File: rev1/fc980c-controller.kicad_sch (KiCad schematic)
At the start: 35 parts, among them J1 SWD, J2 USB, J3 KEYBOARD, SW1 BOOT0, U1 XC6206P332MR, U2 STM32F401CBUx, U3 USBLC6-2SC6, U4 M24C64-RMN6TP, U5 PCA9306DC, Y1 8MHz Cl 20pF

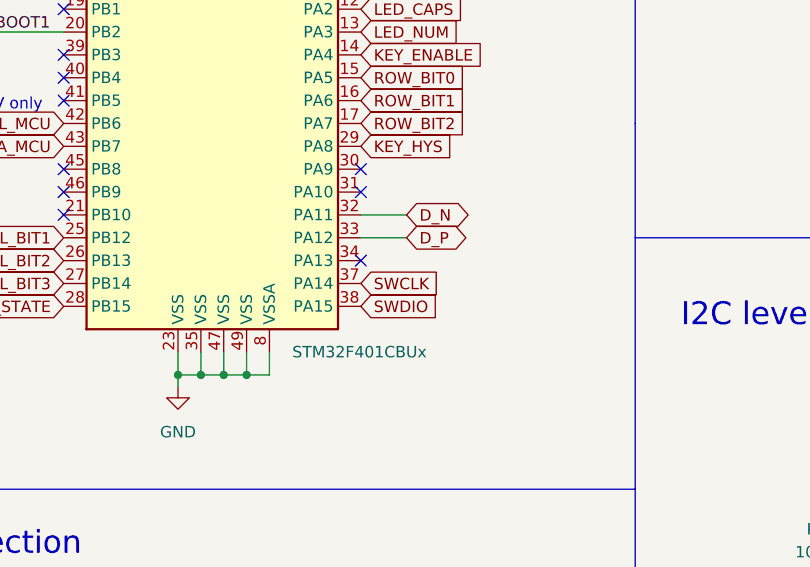
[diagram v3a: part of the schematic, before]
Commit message: rev2: Fix SWDIO MCU pin
Didn't take long to find flaws in the revision 1 design. SWDIO is
erroneously hooked up to PA15 on the MCU instead of PA13.
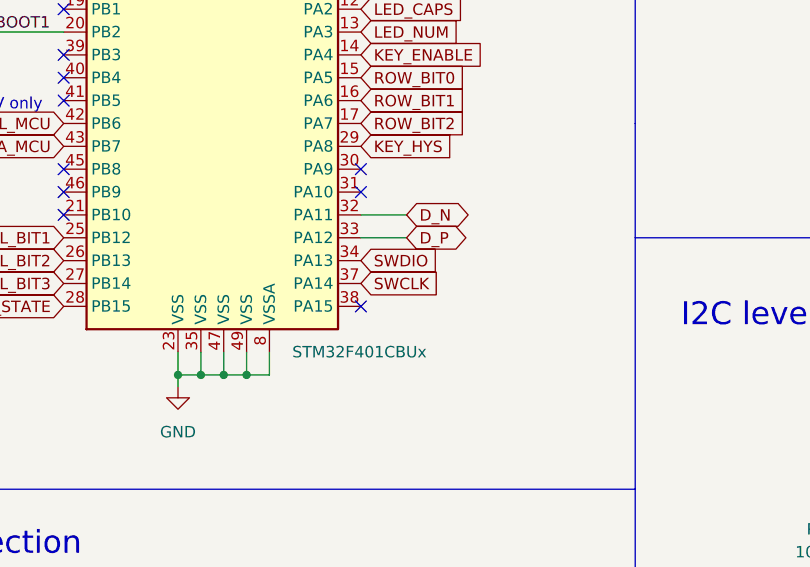
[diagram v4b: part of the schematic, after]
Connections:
- net SWDIO: now also U2.34 (PA13); no longer U2.38 (PA15)
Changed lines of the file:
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@@
   )
   (no_connect (at 74.93 64.77))
+  (no_connect (at 74.93 102.87))
   (no_connect (at 41.91 62.23))
   (no_connect (at 41.91 57.15))
@@
   (no_connect (at 41.91 77.47))
   (no_connect (at 41.91 74.93))
-  (no_connect (at 74.93 97.79))
   (no_connect (at 41.91 87.63))
   (no_connect (at 41.91 90.17))
@@
     )
   )
-  (global_label "SWDIO" (shape input) (at 74.93 102.87 0) (fields_autoplaced)
-    (effects (font (size 1.27 1.27)) (justify left))
-    (property "Intersheet References" "${INTERSHEET_REFS}" (id 0) (at 83.2093 102.7906 0)
-      (effects (font (size 1.27 1.27)) (justify left) hide)
-    )
-  )
   (global_label "I2C_SDA_MCU" (shape input) (at 41.91 85.09 180) (fields_autoplaced)
     (effects (font (size 1.27 1.27)) (justify right))
@@
     (effects (font (size 1.27 1.27)) (justify left))
     (property "Intersheet References" "${INTERSHEET_REFS}" (id 0) (at 216.4383 69.7706 0)
+      (effects (font (size 1.27 1.27)) (justify left) hide)
+    )
+  )
+  (global_label "SWDIO" (shape input) (at 74.93 97.79 0) (fields_autoplaced)
+    (effects (font (size 1.27 1.27)) (justify left))
+    (property "Intersheet References" "${INTERSHEET_REFS}" (id 0) (at 83.2093 97.7106 0)
       (effects (font (size 1.27 1.27)) (justify left) hide)
     )
@@
       (effects (font (size 1.27 1.27)) (justify right) hide)
     )
-    (property "Datasheet" "http://www.st.com/st-web-ui/static/active/en/resource/technical/document/datasheet/DM00086815.pdf" (id 3) (at 59.69 67.31 0)
-      (effects (font (size 1.27 1.27)) hide)
-    )
+    (property "Datasheet" "https://datasheet.lcsc.com/lcsc/1809032024_STMicroelectronics-STM32F401CBU6_C118825.pdf" (id 3) (at 59.69 67.31 0)
+      (effects (font (size 1.27 1.27)) hide)
+    )

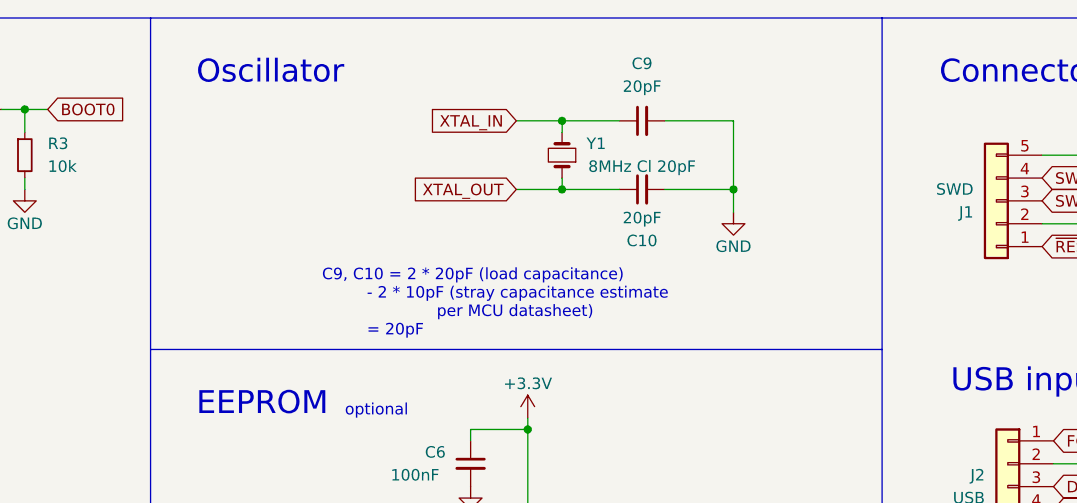
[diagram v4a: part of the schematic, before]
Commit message: rev2: Explain oscillator frequency choice
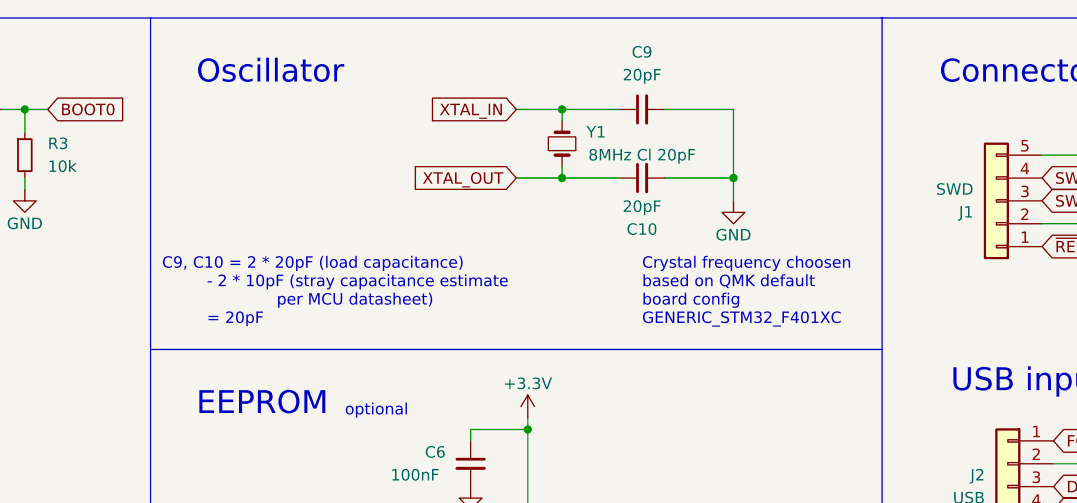
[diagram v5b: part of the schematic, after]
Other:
- note added: "Crystal frequency choosen based on QMK default board config GENERIC_STM32_F401XC"
- moved on the sheet: C10, C9, Y1
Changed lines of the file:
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@@
   (junction (at 62.23 110.49) (diameter 0) (color 0 0 0 0)
   )
-  (junction (at 170.18 34.29) (diameter 0) (color 0 0 0 0)
-  )
-  (junction (at 151.13 26.67) (diameter 0) (color 0 0 0 0)
+  (junction (at 170.18 33.02) (diameter 0) (color 0 0 0 0)
+  )
+  (junction (at 151.13 25.4) (diameter 0) (color 0 0 0 0)
   )
   (junction (at 267.97 125.73) (diameter 0) (color 0 0 0 0)
@@
   (junction (at 147.32 60.96) (diameter 0) (color 0 0 0 0)
   )
-  (junction (at 151.13 34.29) (diameter 0) (color 0 0 0 0)
+  (junction (at 151.13 33.02) (diameter 0) (color 0 0 0 0)
   )
   (junction (at 205.74 100.33) (diameter 0) (color 0 0 0 0)
@@
     (stroke (width 0) (type default) (color 0 0 0 0))
   )
-  (wire (pts (xy 170.18 36.83) (xy 170.18 34.29))
+  (wire (pts (xy 170.18 35.56) (xy 170.18 33.02))
     (stroke (width 0) (type default) (color 0 0 0 0))
   )
@@
     (stroke (width 0) (type default) (color 0 0 0 0))
   )
-  (wire (pts (xy 146.05 26.67) (xy 151.13 26.67))
+  (wire (pts (xy 146.05 25.4) (xy 151.13 25.4))
     (stroke (width 0) (type default) (color 0 0 0 0))
   )
@@
     (stroke (width 0) (type default) (color 0 0 0 0))
   )
-  (wire (pts (xy 151.13 33.02) (xy 151.13 34.29))
+  (wire (pts (xy 151.13 31.75) (xy 151.13 33.02))
     (stroke (width 0) (type default) (color 0 0 0 0))
   )
@@
     (stroke (width 0) (type default) (color 0 0 0 0))
   )
-  (wire (pts (xy 170.18 34.29) (xy 162.56 34.29))
+  (wire (pts (xy 170.18 33.02) (xy 162.56 33.02))
     (stroke (width 0) (type default) (color 0 0 0 0))
   )
@@
     (stroke (width 0) (type default) (color 0 0 0 0))
   )
-  (wire (pts (xy 162.56 26.67) (xy 170.18 26.67))
+  (wire (pts (xy 162.56 25.4) (xy 170.18 25.4))
     (stroke (width 0) (type default) (color 0 0 0 0))
   )
@@
     (stroke (width 0) (type default) (color 0 0 0 0))
   )
-  (wire (pts (xy 170.18 26.67) (xy 170.18 34.29))
+  (wire (pts (xy 170.18 25.4) (xy 170.18 33.02))
     (stroke (width 0) (type default) (color 0 0 0 0))
   )
@@
     (stroke (width 0) (type default) (color 0 0 0 0))
   )
-  (wire (pts (xy 151.13 26.67) (xy 157.48 26.67))
+  (wire (pts (xy 151.13 25.4) (xy 157.48 25.4))
     (stroke (width 0) (type default) (color 0 0 0 0))
   )
@@
     (stroke (width 0) (type default) (color 0 0 0 0))
   )
-  (wire (pts (xy 151.13 26.67) (xy 151.13 27.94))
+  (wire (pts (xy 151.13 25.4) (xy 151.13 26.67))
     (stroke (width 0) (type default) (color 0 0 0 0))
   )
@@
     (stroke (width 0) (type default) (color 0 0 0 0))
   )
-  (wire (pts (xy 151.13 34.29) (xy 157.48 34.29))
+  (wire (pts (xy 151.13 33.02) (xy 157.48 33.02))
     (stroke (width 0) (type default) (color 0 0 0 0))
   )
@@
     (stroke (width 0) (type default) (color 0 0 0 0))
   )
-  (wire (pts (xy 146.05 34.29) (xy 151.13 34.29))
+  (wire (pts (xy 146.05 33.02) (xy 151.13 33.02))
     (stroke (width 0) (type default) (color 0 0 0 0))
   )
@@
   )
   (text "C9, C10 = 2 * 20pF (load capacitance)\n         - 2 * 10pF (stray capacitance estimate\n                       per MCU datasheet)\n         = 20pF"
-    (at 124.46 50.8 0)
+    (at 106.68 49.53 0)
     (effects (font (size 1.27 1.27)) (justify left bottom))
   )
@@
   (text "I2C on the keyboard side is pulled up to 5V,\noriginal controller connects MCU (3.3V, 5V tolerant) directly,\nseems a bit sketchy\n"
     (at 121.285 160.02 0)
+    (effects (font (size 1.27 1.27)) (justify left bottom))
+  )
+  (text "Crystal frequency choosen\nbased on QMK default\nboard config\nGENERIC_STM32_F401XC"
+    (at 160.02 49.53 0)
     (effects (font (size 1.27 1.27)) (justify left bottom))
   )
@@
     )
   )
-  (global_label "XTAL_IN" (shape input) (at 146.05 26.67 180) (fields_autoplaced)
+  (global_label "XTAL_IN" (shape input) (at 146.05 25.4 180) (fields_autoplaced)
     (effects (font (size 1.27 1.27)) (justify right))
-    (property "Intersheet References" "${INTERSHEET_REFS}" (id 0) (at 136.4402 26.5906 0)
+    (property "Intersheet References" "${INTERSHEET_REFS}" (id 0) (at 136.4402 25.3206 0)
       (effects (font (size 1.27 1.27)) (justify right) hide)
     )
@@
     )
   )
-  (global_label "XTAL_OUT" (shape input) (at 146.05 34.29 180) (fields_autoplaced)
+  (global_label "XTAL_OUT" (shape input) (at 146.05 33.02 180) (fields_autoplaced)
     (effects (font (size 1.27 1.27)) (justify right))
-    (property "Intersheet References" "${INTERSHEET_REFS}" (id 0) (at 134.7469 34.2106 0)
+    (property "Intersheet References" "${INTERSHEET_REFS}" (id 0) (at 134.7469 32.9406 0)
       (effects (font (size 1.27 1.27)) (justify right) hide)
     )
@@
     (pin "1")
   )
-  (symbol (lib_id "power:GND") (at 170.18 36.83 0) (unit 1)
-    (in_bom yes) (on_board yes)
-    (property "Reference" "#PWR026" (id 0) (at 170.18 43.18 0)
-      (effects (font (size 1.27 1.27)) hide)
-    )
-    (property "Value" "GND" (id 1) (at 170.18 40.64 0))
-    (property "Footprint" "" (id 2) (at 170.18 36.83 0)
-      (effects (font (size 1.27 1.27)) hide)
-    )
-    (property "Datasheet" "" (id 3) (at 170.18 36.83 0)
+  (symbol (lib_id "power:GND") (at 170.18 35.56 0) (unit 1)
+    (in_bom yes) (on_board yes)
+    (property "Reference" "#PWR026" (id 0) (at 170.18 41.91 0)
+      (effects (font (size 1.27 1.27)) hide)
+    )
+    (property "Value" "GND" (id 1) (at 170.18 39.37 0))
+    (property "Footprint" "" (id 2) (at 170.18 35.56 0)
+      (effects (font (size 1.27 1.27)) hide)
+    )
+    (property "Datasheet" "" (id 3) (at 170.18 35.56 0)
       (effects (font (size 1.27 1.27)) hide)
     )
@@
     (pin "1")
   )
-  (symbol (lib_id "Device:C_Small") (at 160.02 26.67 90) (unit 1)
-    (in_bom yes) (on_board yes) (fields_autoplaced)
-    (property "Reference" "C9" (id 0) (at 160.0263 20.32 90))
-    (property "Value" "20pF" (id 1) (at 160.0263 22.86 90))
-    (property "Footprint" "Capacitor_SMD:C_0402_1005Metric" (id 2) (at 160.02 26.67 0)
-      (effects (font (size 1.27 1.27)) hide)
-    )
-    (property "Datasheet" "~" (id 3) (at 160.02 26.67 0)
+  (symbol (lib_id "Device:C_Small") (at 160.02 25.4 90) (unit 1)
+    (in_bom yes) (on_board yes) (fields_autoplaced)
+    (property "Reference" "C9" (id 0) (at 160.0263 19.05 90))
+    (property "Value" "20pF" (id 1) (at 160.0263 21.59 90))
+    (property "Footprint" "Capacitor_SMD:C_0402_1005Metric" (id 2) (at 160.02 25.4 0)
+      (effects (font (size 1.27 1.27)) hide)
+    )
+    (property "Datasheet" "~" (id 3) (at 160.02 25.4 0)
       (effects (font (size 1.27 1.27)) hide)
     )
@@
     (pin "9")
   )
-  (symbol (lib_id "Device:Crystal_Small") (at 151.13 30.48 90) (unit 1)
-    (in_bom yes) (on_board yes)
-    (property "Reference" "Y1" (id 0) (at 154.94 29.21 90))
-    (property "Value" "8MHz Cl 20pF" (id 1) (at 160.02 31.75 90))
-    (property "Footprint" "Crystal:Crystal_SMD_5032-2Pin_5.0x3.2mm" (id 2) (at 151.13 30.48 0)
-      (effects (font (size 1.27 1.27)) hide)
-    )
-    (property "Datasheet" "https://datasheet.lcsc.com/lcsc/2103291135_Yangxing-Tech-X50328MSB2GI_C115962.pdf" (id 3) (at 151.13 30.48 0)
+  (symbol (lib_id "Device:Crystal_Small") (at 151.13 29.21 90) (unit 1)
+    (in_bom yes) (on_board yes)
+    (property "Reference" "Y1" (id 0) (at 154.94 27.94 90))
+    (property "Value" "8MHz Cl 20pF" (id 1) (at 160.02 30.48 90))
+    (property "Footprint" "Crystal:Crystal_SMD_5032-2Pin_5.0x3.2mm" (id 2) (at 151.13 29.21 0)
+      (effects (font (size 1.27 1.27)) hide)
+    )
+    (property "Datasheet" "https://datasheet.lcsc.com/lcsc/2103291135_Yangxing-Tech-X50328MSB2GI_C115962.pdf" (id 3) (at 151.13 29.21 0)
       (effects (font (size 1.27 1.27)) hide)
     )
@@
     (pin "8")
   )
-  (symbol (lib_id "Device:C_Small") (at 160.02 34.29 90) (unit 1)
-    (in_bom yes) (on_board yes)
-    (property "Reference" "C10" (id 0) (at 160.02 40.005 90))
-    (property "Value" "20pF" (id 1) (at 160.02 37.465 90))
-    (property "Footprint" "Capacitor_SMD:C_0402_1005Metric" (id 2) (at 160.02 34.29 0)
-      (effects (font (size 1.27 1.27)) hide)
-    )
-    (property "Datasheet" "~" (id 3) (at 160.02 34.29 0)
-      (effects (font (size 1.27 1.27)) hide)
-    )
+  (symbol (lib_id "Device:C_Small") (at 160.02 33.02 90) (unit 1)
+    (in_bom yes) (on_board yes)
+    (property "Reference" "C10" (id 0) (at 160.02 38.735 90))
+    (property "Value" "20pF" (id 1) (at 160.02 36.195 90))
+    (property "Footprint" "Capacitor_SMD:C_0402_1005Metric" (id 2) (at 160.02 33.02 0)
+      (effects (font (size 1.27 1.27)) hide)
+    )
+    (property "Datasheet" "~" (id 3) (at 160.02 33.02 0)
+      (effects (font (size 1.27 1.27)) hide)
+    )

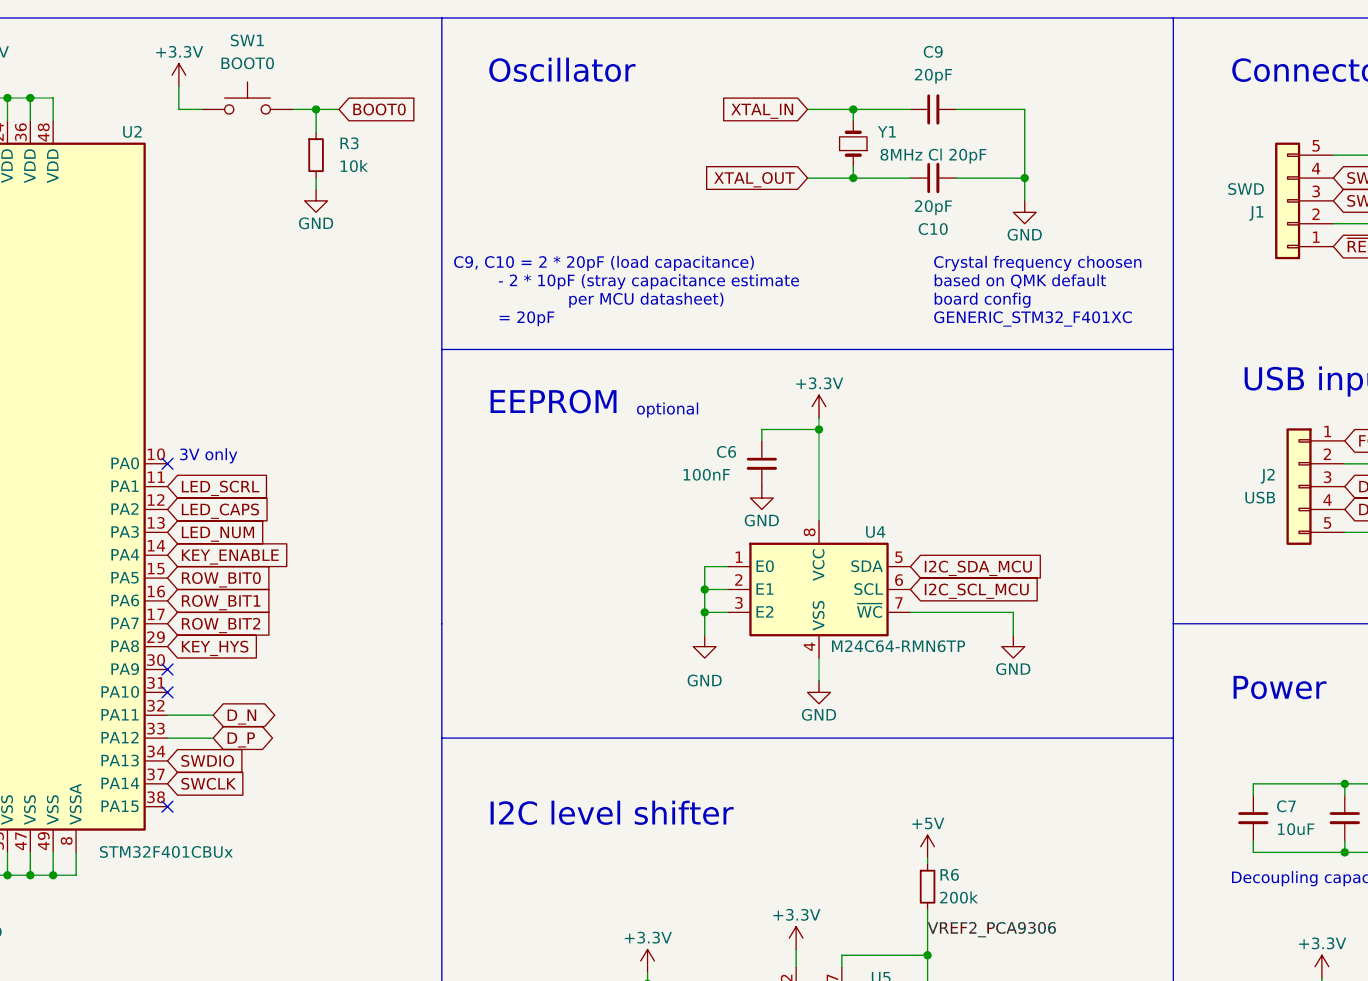
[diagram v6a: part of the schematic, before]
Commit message: rev1: Revert rev2 changes
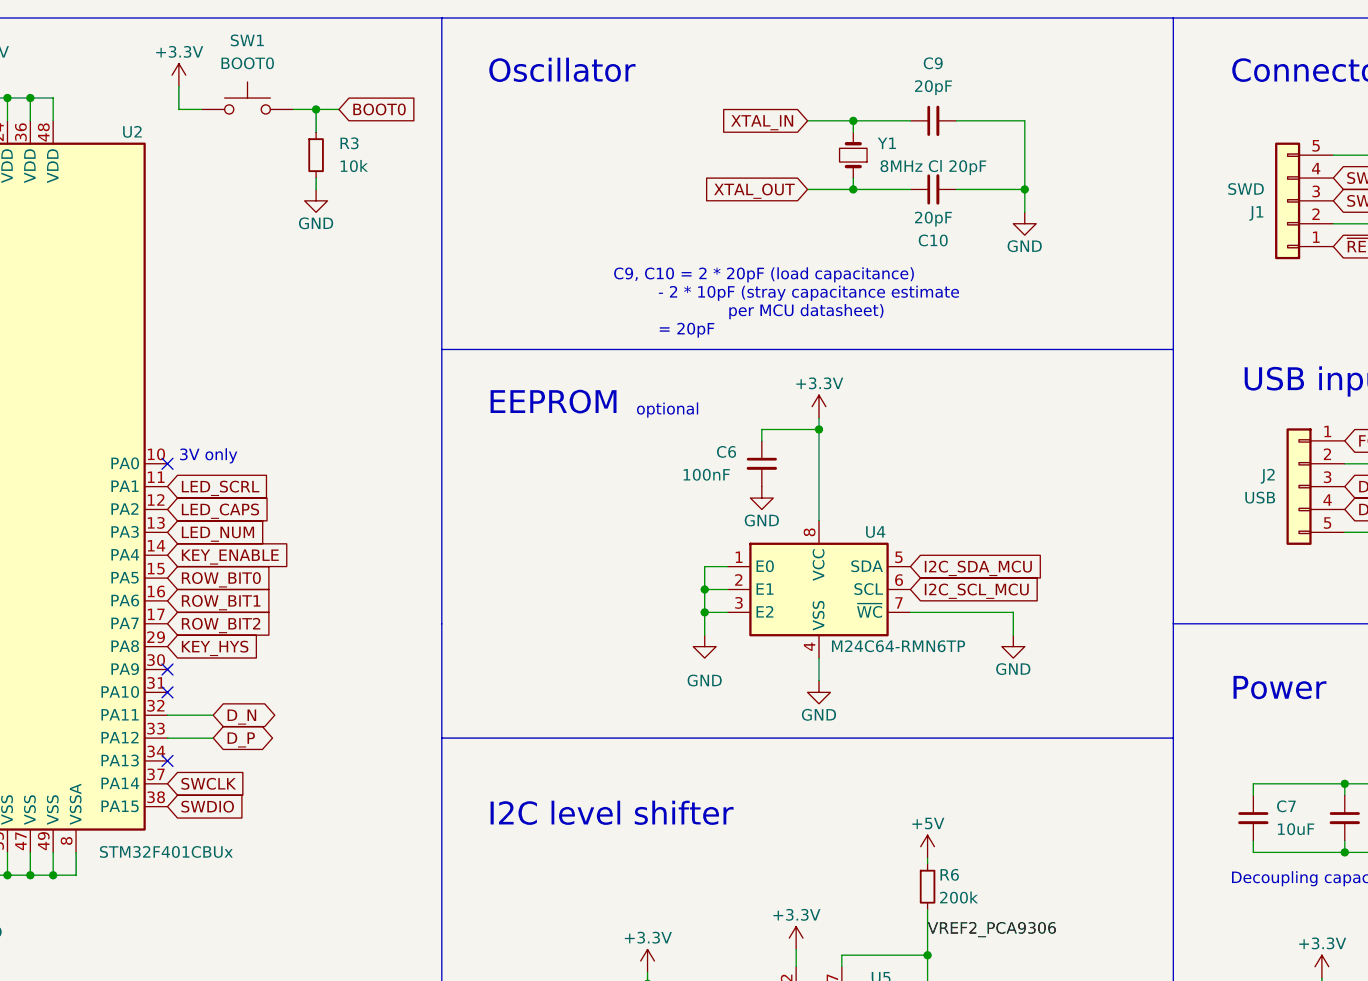
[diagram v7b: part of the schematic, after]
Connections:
- net SWDIO: now also U2.38 (PA15); no longer U2.34 (PA13)
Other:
- note removed: "Crystal frequency choosen based on QMK default board config GENERIC_STM32_F401XC"
- moved on the sheet: C10, C9, Y1
